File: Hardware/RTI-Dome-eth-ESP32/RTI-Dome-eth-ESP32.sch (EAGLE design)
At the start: 96 parts, among them IC1 LM2675MX-5.0_NOPB, IC2 24LC64T-I/SN, IC8 REG1117-3.3V, J1 691313510003, J10 691313510002, J11 691313510002, J12 691313510002, J2 XT60PW-M, J3 691313510003, J4 691313510003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

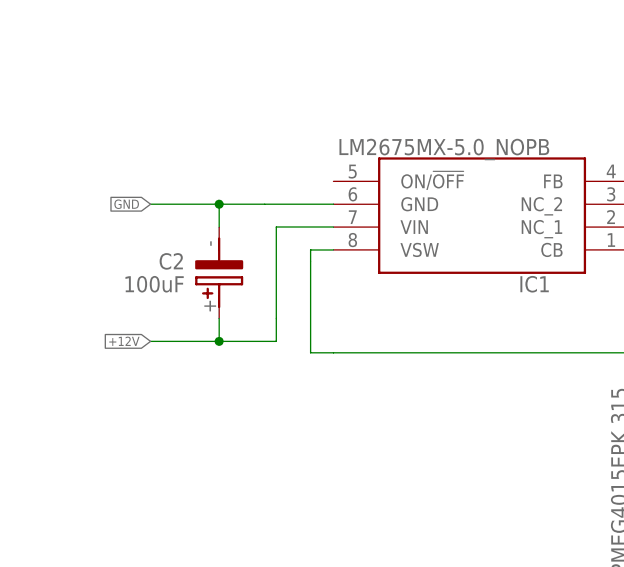
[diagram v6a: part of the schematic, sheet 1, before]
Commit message: New ESP32 firmware is working.
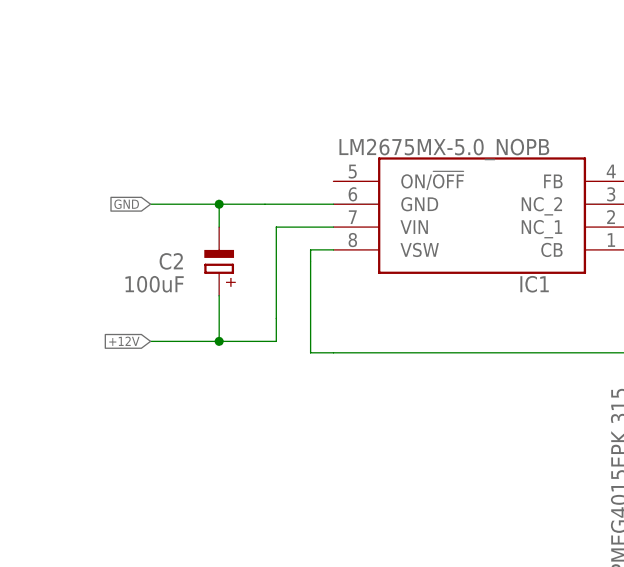
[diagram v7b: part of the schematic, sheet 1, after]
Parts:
- C2: device samacsys:MAL215099804E3"" -> rcl:CPOL-EUUD-6,3X7,7; JLCPCB (none) -> VZH101M1VTR-0607; MPN C249838 -> VZH101M1VTR-0607
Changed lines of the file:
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@@
 <attribute name="MPN" value="RT0805FRE074K7L"/>
 </part>
-<part name="U2" library="ESP32-DEVKITC-32D" library_urn="urn:adsk.eagle:library:44270575" deviceset="ESP32-DEVKITC-32" device="U" package3d_urn="urn:adsk.eagle:package:44294361/4" value="ESP32-DevKitC-32UE"/>
-<part name="JP1" library="rti" library_urn="urn:adsk.eagle:library:37256580" deviceset="JP2E" device="" package3d_urn="urn:adsk.eagle:package:37318384/1"/>
+<part name="U2" library="ESP32-DEVKITC-32D" library_urn="urn:adsk.eagle:library:44270575" deviceset="ESP32-DEVKITC-32" device="U" package3d_urn="urn:adsk.eagle:package:44294361/7" value="ESP32-DevKitC-32UE"/>
+<part name="JP1" library="rti" library_urn="urn:adsk.eagle:library:37256580" deviceset="JP2E" device="" package3d_urn="urn:adsk.eagle:package:37318384/2"/>
 <part name="GND6" library="supply1" library_urn="urn:adsk.eagle:library:371" deviceset="GND" device=""/>
 <part name="J1" library="samacsys" library_urn="urn:adsk.eagle:library:37256869" deviceset="691313510003" device="" package3d_urn="urn:adsk.eagle:package:45454765/2"/>
@@
 <part name="IC1" library="samacsys" library_urn="urn:adsk.eagle:library:37256869" deviceset="LM2675MX-5.0_NOPB" device="" package3d_urn="urn:adsk.eagle:package:45493951/5"/>
 <part name="D1" library="samacsys" library_urn="urn:adsk.eagle:library:37256869" deviceset="PMEG4015EPK,315" device="" package3d_urn="urn:adsk.eagle:package:45493982/4"/>
-<part name="C2" library="samacsys" library_urn="urn:adsk.eagle:library:37256869" deviceset="MAL215099804E3" device="&quot;&quot;" package3d_urn="urn:adsk.eagle:package:38013982/9" value="100uF">
-<attribute name="MPN" value="C249838"/>
+<part name="C2" library="rcl" library_urn="urn:adsk.eagle:library:334" deviceset="CPOL-EU" device="UD-6,3X7,7" package3d_urn="urn:adsk.eagle:package:23472/1" value="100uF">
+<spice>
+<pinmapping spiceprefix="C">
+<pinmap gate="G$1" pin="+" pinorder="1"/>
+<pinmap gate="G$1" pin="-" pinorder="2"/>
+</pinmapping>
+</spice>
+<attribute name="JLCPCB" value="VZH101M1VTR-0607"/>
+<attribute name="MPN" value="VZH101M1VTR-0607
+"/>
 </part>
 <part name="C3" library="samacsys" library_urn="urn:adsk.eagle:library:37256869" deviceset="EEE-FP1C680AL" device="" package3d_urn="urn:adsk.eagle:package:45493987/6" value="68uF"/>
@@
 <attribute name="VALUE" x="31.75" y="60.96" size="1.778" layer="96" rot="R180" align="center-left"/>
 <attribute name="MPN" x="35.56" y="62.23" size="1.778" layer="96" rot="R180" display="off"/>
+<attribute name="JLCPCB" x="35.56" y="62.23" size="1.778" layer="96" rot="R180" display="off"/>
 </instance>
 <instance part="C3" gate="G$1" x="106.68" y="44.45" smashed="yes" rot="R270">
@@
 <pinref part="C2" gate="G$1" pin="+"/>
 <wire x1="35.56" y1="54.61" x2="27.94" y2="54.61" width="0.1524" layer="91"/>
-<wire x1="35.56" y1="57.15" x2="35.56" y2="54.61" width="0.1524" layer="91"/>
+<wire x1="35.56" y1="59.69" x2="35.56" y2="54.61" width="0.1524" layer="91"/>
 <junction x="35.56" y="54.61"/>
 <label x="27.94" y="54.61" size="1.016" layer="95" rot="R180" xref="yes"/>
